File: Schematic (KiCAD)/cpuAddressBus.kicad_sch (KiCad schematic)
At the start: 150 parts, among them J1 INVERT, J10 INVERT, J11 NAND_4, J12 INVERT, J13 NAND_4, J16 INVERT, J17 NAND_4, J18 INVERT, J19 NAND_4, J20 INVERT, J21 NAND_4, J22 INVERT, J23 NAND_4, J24 INVERT, J25 NAND_4, J26 INVERT, J27 NAND_4, J28 INVERT, J29 NAND_4, J30 INVERT, J31 NAND_4, J32 INVERT, J33 NAND_4, J34 INVERT, J35 NAND_4, J36 INVERT, J37 NAND_4, J38 INVERT, J39 NAND_4, J40 INVERT, J41 NAND_4, J42 INVERT, J43 NAND_2, J44 INVERT, J45 NAND_4, J46 INVERT, J47 NAND_4, J48 INVERT, J49 NAND_4, J50 INVERT, J51 NAND_3, J52 INVERT, J53 NAND_3, J54 INVERT, J55 NAND_3, J59 INVERT, J9 NAND_4, K1 INVERT, K18 INVERT, K2 INVERT, K25 INVERT, K27 INVERT, K3 INVERT, K30 INVERT, K34 INVERT, K36 INVERT, K37 INVERT, K39 INVERT, K4 INVERT, K44 INVERT, K47 INVERT, K48 INVERT, K5 NAND_3, K51 INVERT, K53 INVERT, K55 INVERT, K57 INVERT, K59 INVERT, K6 NAND_4, K63 INVERT, K68 INVERT, K70 INVERT, K74 INVERT, K82 INVERT, K84 INVERT, K88 INVERT, K89 INVERT, K90 INVERT, K98 INVERT, M2_Pinbuf_1 BUFFER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

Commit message: Tracing and schematic updates.  - Added timer to schematic.  - Added all items from artifacts sheet to the MMC5A trace.
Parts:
- removed E14.2, E23,E24: BIGBUF, symbol MMC5:BIGBUF
- removed E15: INVERT, symbol MMC5:INVERT
- added GH1: NAND_2, symbol MMC5:NAND_2
- added GH2, J71: INVERT, symbol MMC5:INVERT
- added J3: BUF 83, symbol MMC5:BIGBUF
- added PinBuf: BUFFER, symbol MMC5:BUFFER
- H1: value BIGBUF -> BUF 83
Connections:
- net +CPU_A11{H25}: now also GH1. (X)
- net +M2_CLK_BUF3{H34}: now also J3. (X)
- net /CPU_$x2xx{J45}: now also J71. (X)
- net /CPU_A10{H24}: now also GH1. (X)
- net /ROMSEL_Pin: now also PinBuf. (X); no longer H33. (X)
- net M2_Slow{J3}: now reaches H1. (X)
- net M2_Slow{J3}: now also K5. (X), K6. (X), J3. (X)
- net /Romsel{PinBuf}: now reaches H33. (X)
- net /Romsel{PinBuf}: now also PinBuf. (X); no longer H36. (X)
- new net: H1. (X), K6. (X)
- new net: H2. (X), K18. (X), K30. (X), K36. (X), K48. (X), K63. (X), K74. (X), K89. (X), K98. (X)
- new net: H34. (X), H35. (X)
- new net: J1. (X), K6. (X)
- new net: H33. (X), H36. (X)
- new net: B109. (X), B110. (X)
- new net +CPU_$x2xx{J71}: J71. (X)
- new net +CPU_$x8xx-xBxx{GH2}: GH2. (X)
- new net /CPU_$x8xx-xBxx{GH1}: GH1. (X), GH2. (X)
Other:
- note added: "BigBuff 83 seems to add a delay to M2 here."
- note added: "MMC5A Only"
- note removed: "Issues seeing traces in this area."
- moved on the sheet: BK88, E27, H1, H2, H33, H36, H37, J1, J43, J44, K1, K18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

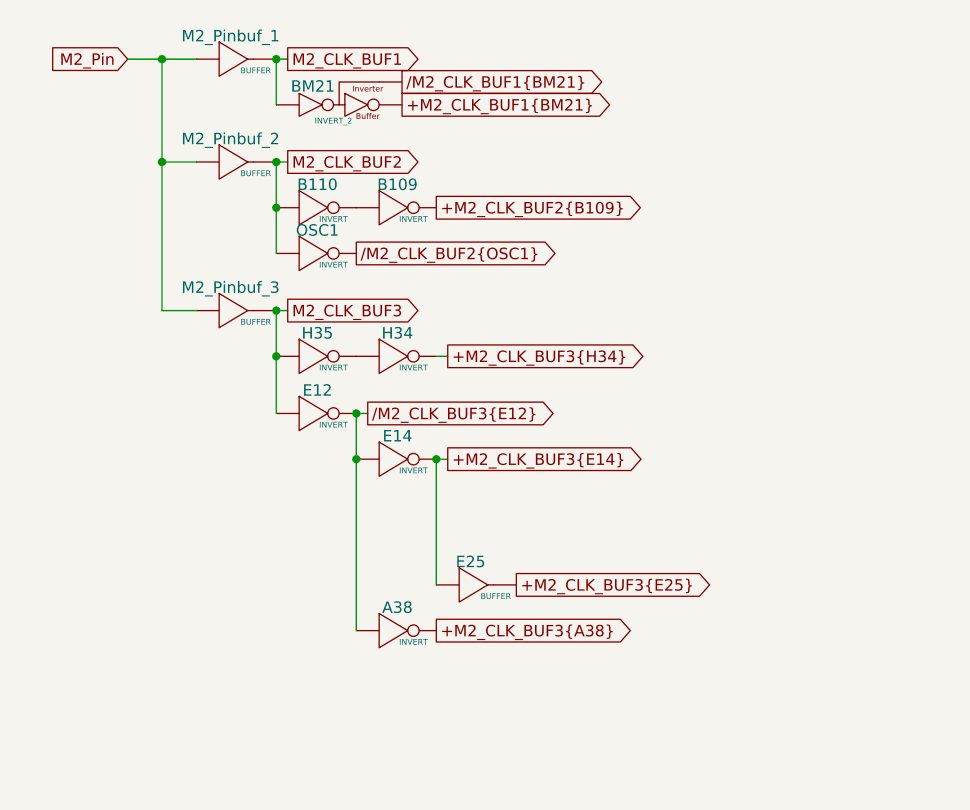
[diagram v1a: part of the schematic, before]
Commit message: - Updated all of the various And-OR-Invert gates to have consistent names.  - Added the schematic for CL3 / SL3 GPIO pins.  There are no surprises revealed by this.  - Finished up the CPU address decoding tracing.  - Added one of the 'artifact' counters from the pulse channels
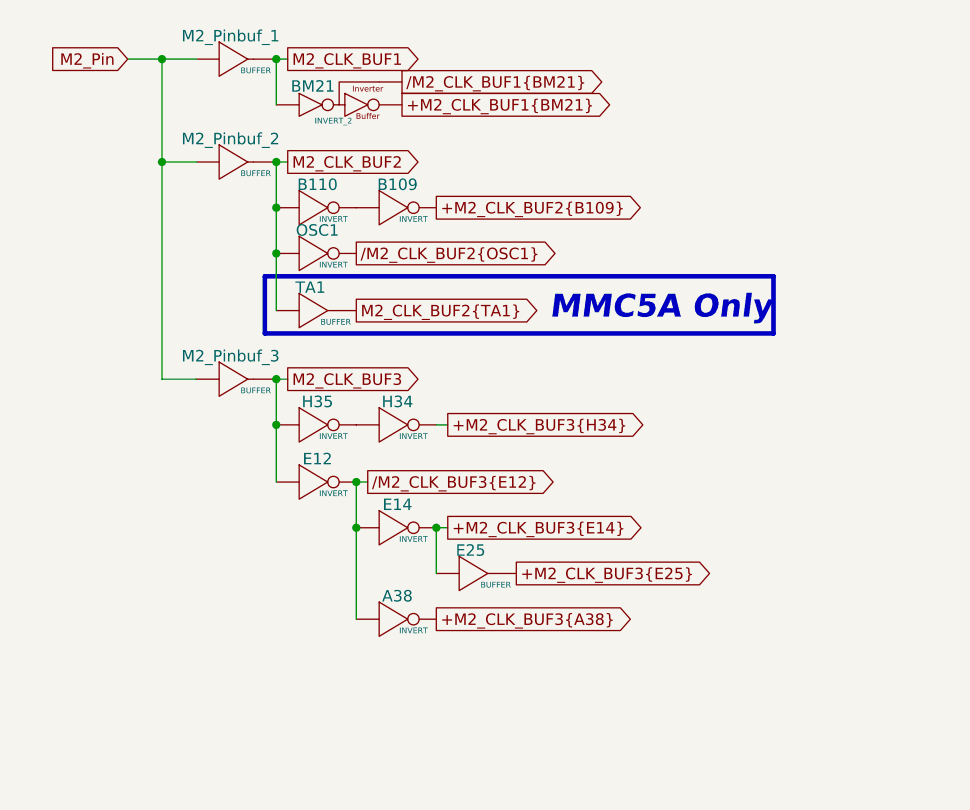
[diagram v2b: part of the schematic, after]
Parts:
- added TA1: BUFFER, symbol MMC5:BUFFER
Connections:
- net M2_CLK_BUF2: now also TA1. (X)
- new net: H1. (X), K6. (X)
- new net: H2. (X), K18. (X), K30. (X), K36. (X), K48. (X), K63. (X), K74. (X), K89. (X), K98. (X)
- new net: H34. (X), H35. (X)
- new net: J1. (X), K6. (X)
- new net: H33. (X), H36. (X)
- new net: B109. (X), B110. (X)
- new net M2_CLK_BUF2{TA1}: TA1. (X)
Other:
- moved on the sheet: A38, E12, E14, E25, H34, H35, M2_Pinbuf_3
